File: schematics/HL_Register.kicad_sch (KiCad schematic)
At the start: 46 parts, among them U1 74LS161, U2 74LS161, U3 74LS245, U4 74LS161, U5 74LS161, U6 74LS245, U7 74LS245

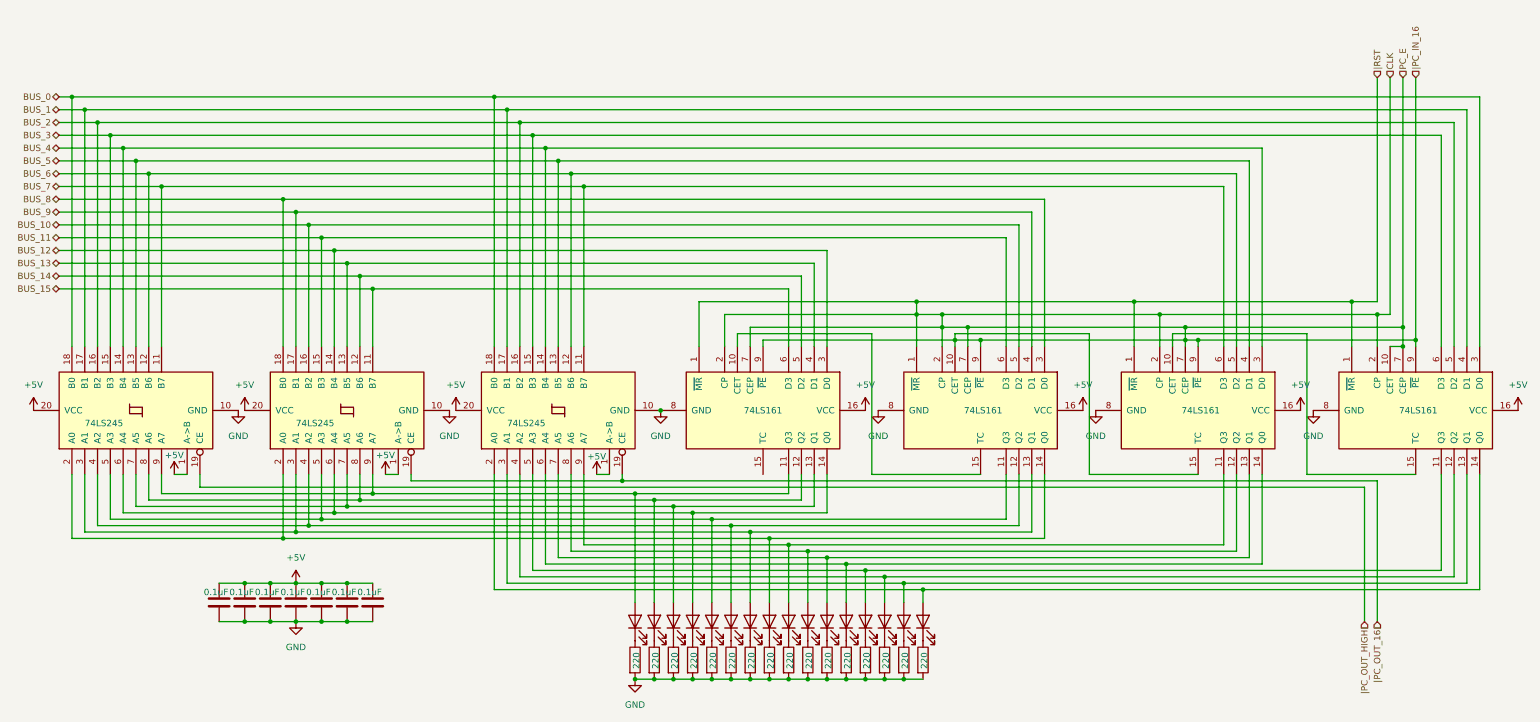
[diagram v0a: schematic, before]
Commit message: feat: updated electrical diagrams & individual part list
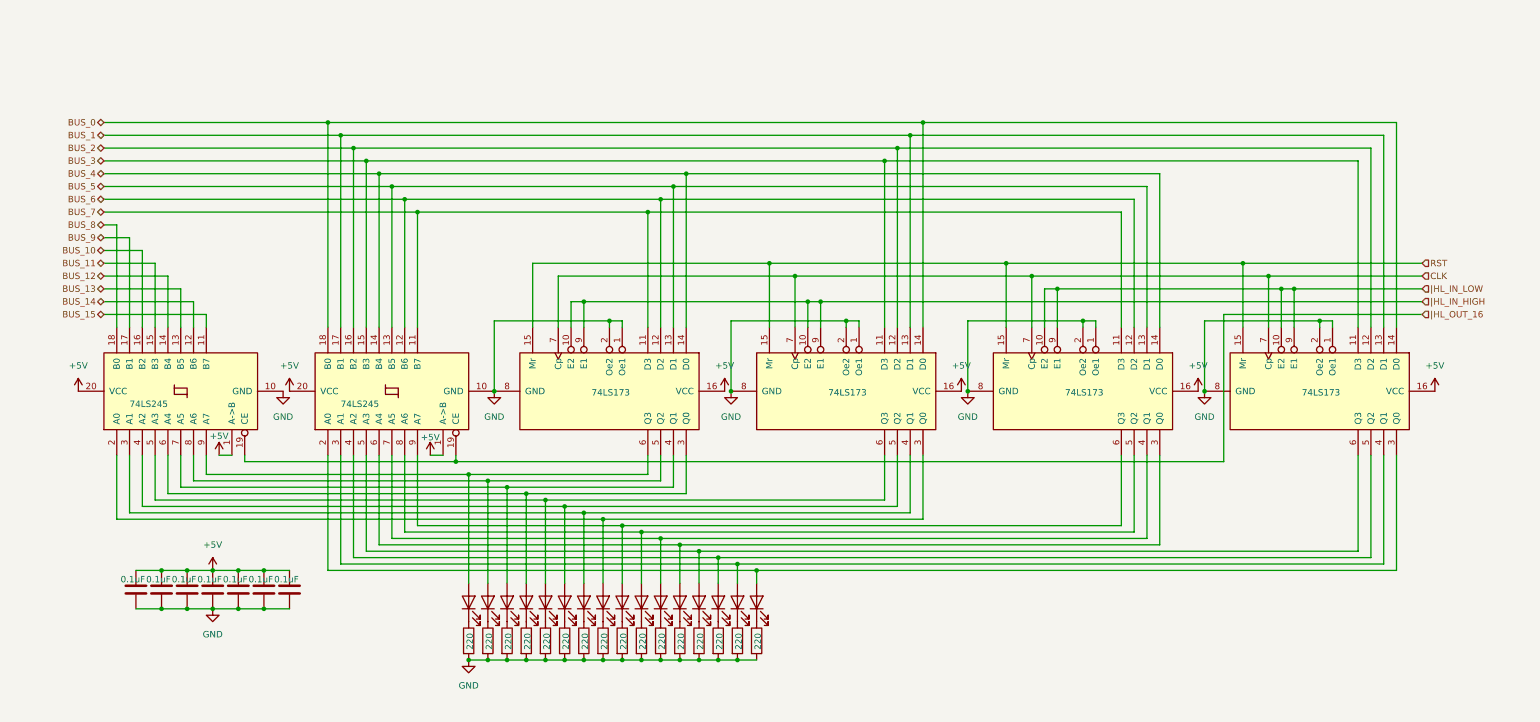
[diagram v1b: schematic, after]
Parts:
- removed U1, U2, U4, U5: 74LS161, symbol 74xx:74LS161
- removed U3: 74LS245, symbol 74xx:74LS245
- added U1, U2, U4, U8: 74LS173, symbol 74xx:74LS173
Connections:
- net +5V: now also U1.16 (VCC), U2.16 (VCC), U4.16 (VCC), U8.16 (VCC)
- net BUS_0: now also U1.14 (D0), U4.14 (D0)
- net BUS_1: now also U1.13 (D1), U4.13 (D1)
- net BUS_2: now also U1.12 (D2), U4.12 (D2)
- net BUS_3: now also U1.11 (D3), U4.11 (D3)
- net BUS_4: now also U2.14 (D0), U8.14 (D0)
- net BUS_5: now also U2.13 (D1), U8.13 (D1)
- net BUS_6: now also U2.12 (D2), U8.12 (D2)
- net BUS_7: now also U2.11 (D3), U8.11 (D3)
- net CLK: now also U1.7 (Cp), U2.7 (Cp), U4.7 (Cp), U8.7 (Cp)
- net GND: now also U1.1 (Oe1), U1.2 (Oe2), U1.8 (GND), U2.1 (Oe1), U2.2 (Oe2), U2.8 (GND), U4.1 (Oe1), U4.2 (Oe2), U4.8 (GND), U8.1 (Oe1), U8.2 (Oe2), U8.8 (GND)
- net at D1.2 (A), U7.9 (A7): now also U8.6 (Q3)
- net at D16.2 (A), U6.2 (A0): now also U4.3 (Q0)
- net at D4.2 (A), U7.6 (A4): now also U8.3 (Q0)
- net at D13.2 (A), U6.5 (A3): now also U4.6 (Q3)
- net at D14.2 (A), U6.4 (A2): now also U4.5 (Q2)
- net at D15.2 (A), U6.3 (A1): now also U4.4 (Q1)
- net at D12.2 (A), U6.6 (A4): now also U2.3 (Q0)
- net at D5.2 (A), U7.5 (A3): now also U1.6 (Q3)
- net at D6.2 (A), U7.4 (A2): now also U1.5 (Q2)
- net at D7.2 (A), U7.3 (A1): now also U1.4 (Q1)
- net at D8.2 (A), U7.2 (A0): now also U1.3 (Q0)
- net at D9.2 (A), U6.9 (A7): now also U2.6 (Q3)
- net at D2.2 (A), U7.8 (A6): now also U8.5 (Q2)
- net at D3.2 (A), U7.7 (A5): now also U8.4 (Q1)
- net at D10.2 (A), U6.8 (A6): now also U2.5 (Q2)
- net at D11.2 (A), U6.7 (A5): now also U2.4 (Q1)
- net |PC_OUT_16 renamed |HL_OUT_16
- new net RST: U1.15 (Mr), U2.15 (Mr), U4.15 (Mr), U8.15 (Mr)
- new net |HL_IN_HIGH: U1.10 (E2), U1.9 (E1), U8.10 (E2), U8.9 (E1)
- new net |HL_IN_LOW: U2.10 (E2), U2.9 (E1), U4.10 (E2), U4.9 (E1)
